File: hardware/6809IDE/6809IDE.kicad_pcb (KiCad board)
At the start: 2 copper layers, 100 x 100 mm, 23 parts, among them J1 SS50-LIKE, J2 Mem Addr, J3 Drive 1, J4 Drive 2, J5 Drive 2, J6 Drive 1, U1 74HC245, U2 74HC245

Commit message: first attempt at FLEX methods
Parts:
- moved ? 23.1 mm to (72.0, 117.0)
- moved C1 23.1 mm to (63.4, 42.5)
- moved C2 23.1 mm to (63.4, 79.3)
- moved D1 23.1 mm to (138.3, 45.0)
- moved D2 23.1 mm to (138.3, 117.4)
- moved D3 23.1 mm to (138.3, 103.4)
- moved D4 23.1 mm to (138.3, 59.0)
- moved H1 23.1 mm to (140.8, 126.3)
- moved H2 23.1 mm to (140.8, 36.1)
- moved H3 23.1 mm to (50.7, 126.3)
- moved H4 23.1 mm to (50.7, 36.1)
- moved J1 23.1 mm to (50.7, 51.3)
- moved J2 23.1 mm to (52.0, 45.0)
- moved J3 23.1 mm to (85.0, 38.6)
- moved J4 23.1 mm to (85.0, 126.3)
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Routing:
- added copper zone on B.Cu, net GND
- added copper zone on F.Cu, net GND

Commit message: move to 1 FLEX sector per IDE sector
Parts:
- J3, J6: value Drive 1 -> Drive 0
- J4, J5: value Drive 2 -> Drive 1

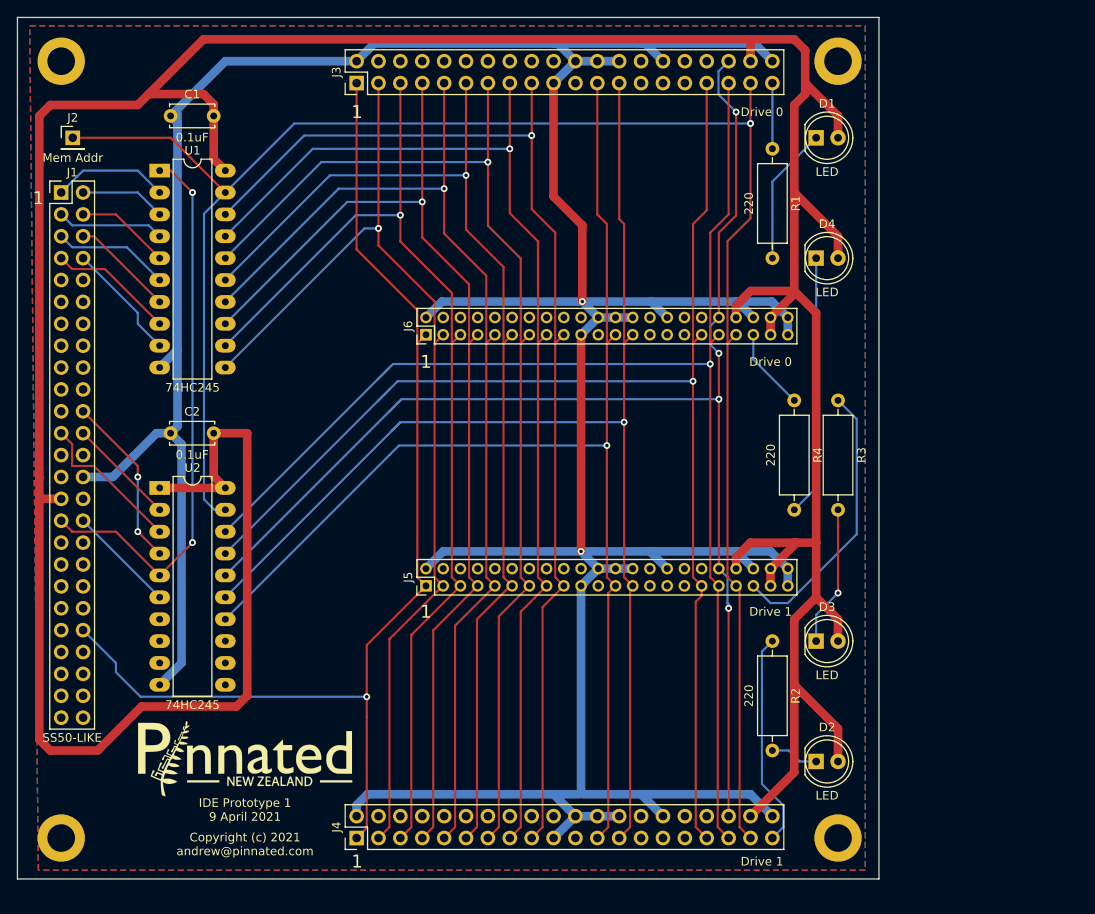
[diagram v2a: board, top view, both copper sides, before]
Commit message: move to single connector
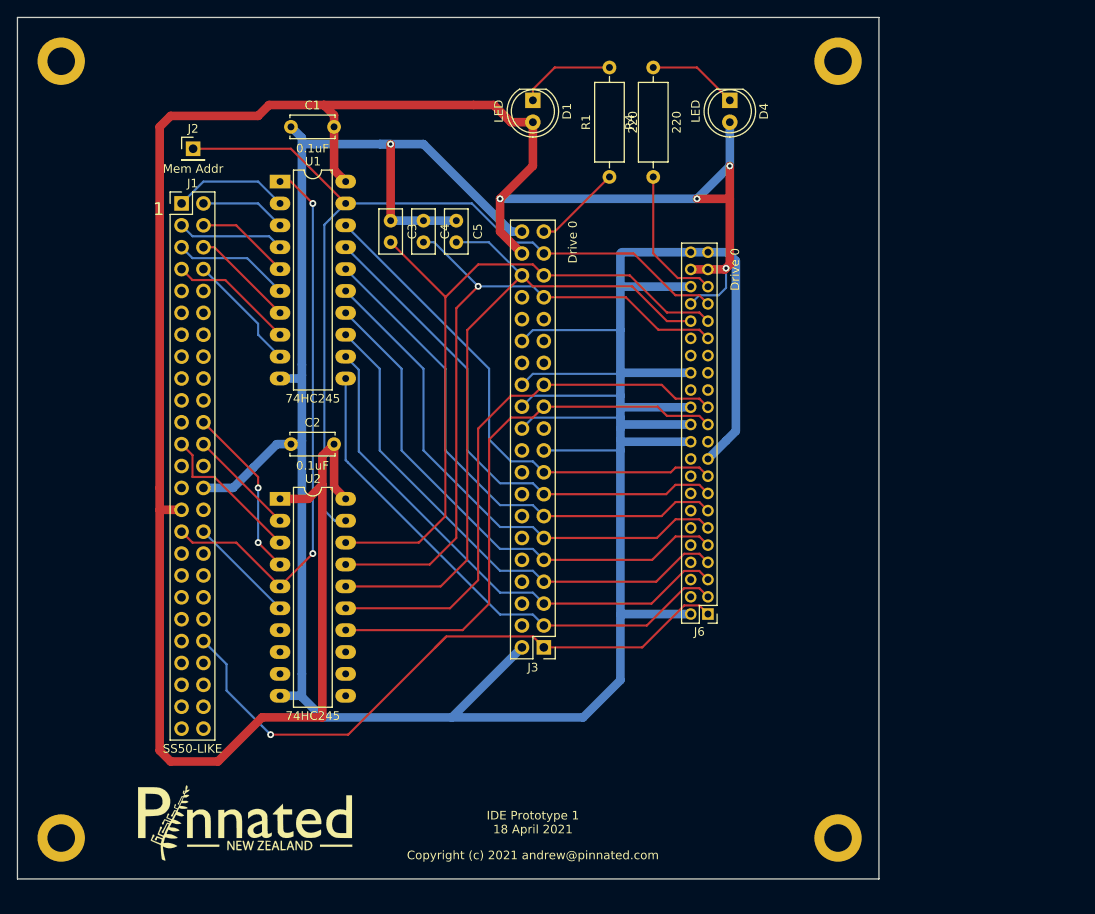
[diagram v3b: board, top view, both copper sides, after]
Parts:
- removed D2, D3: LED, LED_THT:LED_D5.0mm
- removed J4: Drive 1, Connector_PinHeader_2.54mm:PinHeader_2x20_P2.54mm_Vertical
- removed J5: Drive 1, Connector_PinHeader_2.00mm:PinHeader_2x22_P2.00mm_Vertical
- removed R2, R3: 220, Resistor_THT:R_Axial_DIN0309_L9.0mm_D3.2mm_P12.70mm_Horizontal
- added C3: 15pF, Capacitor_THT:C_Disc_D5.0mm_W2.5mm_P2.50mm, F.Cu at (88.9, 54.6)
- added C4: 15pF, Capacitor_THT:C_Disc_D5.0mm_W2.5mm_P2.50mm, F.Cu at (92.7, 54.6)
- added C5: 15pF, Capacitor_THT:C_Disc_D5.0mm_W2.5mm_P2.50mm, F.Cu at (96.5, 54.6)
- moved J3 69.0 mm to (106.7, 104.1), turned to 180 degrees
- moved J6 46.1 mm to (125.7, 100.3), turned to 180 degrees
- moved D1 33.2 mm to (105.4, 40.6), turned to 270 degrees
- moved R4 30.7 mm to (119.4, 49.5), turned to 90 degrees
- moved D4 20.9 mm to (128.3, 40.6), turned to 270 degrees
- moved R1 19.2 mm to (114.3, 49.5), turned to 90 degrees
- moved C1 14.0 mm to (77.3, 43.7)
- moved C2 14.0 mm to (77.3, 80.5)
- moved J1 14.0 mm to (64.6, 52.6)
- moved J2 14.0 mm to (66.0, 46.3)
- moved U1 14.0 mm to (76.1, 50.1)
- moved U2 14.0 mm to (76.1, 86.9)
- moved ? 7.46 mm to (72.0, 124.5)
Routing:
- net +5v: track 424.1 -> 274.7 mm, vias 0 -> 4
- net ~FDD-Select: track 215.5 -> 106.8 mm, vias 1 -> 0
- net ~R: track 146.6 -> 64.2 mm, vias 1 -> 0
- net ~W: track 143.6 -> 64.8 mm, vias 1 -> 0
- net /A2: track 158.8 -> 82.0 mm, vias 4 -> 0
- net /A0: track 157.1 -> 82.0 mm, vias 1 -> 0
- net /A1: track 155.4 -> 82.0 mm
- net /D0: track 131.5 -> 59.4 mm, vias 1 -> 0
- net /D1: track 129.8 -> 60.3 mm, vias 1 -> 0
- net /D2: track 128.1 -> 60.6 mm, vias 1 -> 0
- net /D3: track 126.3 -> 60.8 mm, vias 1 -> 0
- net /D4: track 124.8 -> 61.0 mm, vias 1 -> 0
- net /D5: track 123.2 -> 61.2 mm, vias 1 -> 0
- net GND: track 439.8 -> 379.0 mm, vias 2 -> 1
- net /D6: track 121.6 -> 62.1 mm, vias 1 -> 0
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- removed copper zone on B.Cu, net GND
- removed copper zone on F.Cu, net GND
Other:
- board text added: "IDE Prototype 1 18 April 2021"
- board text removed: "IDE Prototype 1 9 April 2021"

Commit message: start of ROM and RAM board
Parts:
- added J5: Debug, Connector_PinHeader_2.54mm:PinHeader_1x04_P2.54mm_Vertical, F.Cu at (80.3, 118.1)
- J3: value Drive 0 -> 40-pin drive
- J4: renamed from J6; value Drive 0 -> 44-pin rive
- moved ? 53.0 mm to (124.5, 116.8)
- moved J4 2.60 mm to (123.5, 101.5)
- moved C3 2.60 mm to (86.6, 55.9)
- moved D4 2.60 mm to (126.0, 41.9)
- moved J3 2.60 mm to (104.4, 105.4)
- moved C1 2.60 mm to (75.1, 45.0)
- moved C4 2.60 mm to (90.4, 55.9)
- moved C5 2.60 mm to (94.2, 55.9)
- moved J1 2.60 mm to (62.4, 53.9)
- moved J2 2.60 mm to (63.7, 47.5)
- moved U1 2.60 mm to (73.8, 51.3)
- moved C2 2.60 mm to (75.1, 81.8)
- moved D1 2.60 mm to (103.1, 41.9)
- moved R1 2.60 mm to (112.0, 50.8)
- moved R4 2.60 mm to (117.1, 50.8)
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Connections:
- net Net-(J1-Pad31) renamed pre~R
- net Net-(J1-Pad32) renamed pre~W
- J3 pad 37: ~FDD-Select -> ~IDE-Select
- J4 pad 37: ~FDD-Select -> ~IDE-Select
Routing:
- net ~IDE-Select: track 0.00 -> 103.8 mm
- net GND: track 379.0 -> 326.2 mm, vias 1 -> 15
- net ~Reset: track 74.3 -> 103.5 mm, vias 1 -> 0
- net pre~R: track 65.0 -> 88.6 mm
- net pre~W: track 12.6 -> 32.4 mm
- net +5v: track 274.7 -> 290.0 mm
- net ~FDD-Select: track 106.8 -> 91.9 mm
- net Net-(J1-Pad22): vias 2 -> 1
- added copper zone on B.Cu, net GND
- added copper zone on F.Cu, net GND
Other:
- board text added: "IDE Prototype 1 19 April 2021"
- board text removed: "IDE Prototype 1 18 April 2021"
